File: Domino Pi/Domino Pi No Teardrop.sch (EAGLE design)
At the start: 63 parts, among them J1 MH28-1, J2 MH28-1, M1 DOMINO, SW1 IT-1100, U1 MP2162GQH, U2 CP2104-F03-GM, U3 74LVC1G125DCK

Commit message: Changed copyright
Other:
- note added: "The Domino Team may make changes to specifications and product"
- note added: "© 2014, The Domino Team All rights reserved."
- note removed: "Michel Stempin may make changes to specifications and product"
- note removed: "© 2014, Michel Stempin All rights reserved."
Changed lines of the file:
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@@
 <layer number="102" name="CC-BY-SA_Letters" color="0" fill="4" visible="yes" active="yes"/>
 <layer number="103" name="CC-BY-SA_Filling" color="15" fill="1" visible="yes" active="yes"/>
+<layer number="107" name="legend" color="7" fill="1" visible="yes" active="yes"/>
+<layer number="108" name="Module_Measures" color="7" fill="1" visible="yes" active="yes"/>
 <layer number="119" name="mUnrouted" color="7" fill="1" visible="no" active="no"/>
 <layer number="126" name="mbNames" color="7" fill="1" visible="no" active="no"/>
@@
 <text x="302.26" y="12.7" size="0.8128" layer="94">Reference designs are provided "AS IS" and "WITH ALL FAULTS".</text>
 <text x="302.26" y="10.16" size="0.8128" layer="94">regarding this product, including but not limited to, any implied warranties of</text>
-<text x="302.26" y="6.35" size="0.8128" layer="94">Michel Stempin may make changes to specifications and product </text>
+<text x="302.26" y="6.35" size="0.8128" layer="94">The Domino Team may make changes to specifications and product </text>
 <text x="302.26" y="11.43" size="0.8128" layer="94">Global Marine Networks disclaims all other warranties express or implied, </text>
 <text x="302.26" y="8.89" size="0.8128" layer="94">merchantibility or fitness for any particular application.</text>
 <text x="302.26" y="5.08" size="0.8128" layer="94">descriptions at any time, without notice.</text>
-<text x="345.44" y="20.32" size="1.27" layer="94">© 2014, Michel Stempin
+<text x="345.44" y="20.32" size="1.27" layer="94">© 2014, The Domino Team
 All rights reserved.</text>
 <text x="379.222" y="5.334" size="1.778" layer="94">&gt;REV</text>

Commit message: Domino Pi rev. C: removed Schottky diode on +VUSB, it causes too much voltage drop, optimized power wiring, changed Logos
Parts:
- removed D4: BLUE, Domino:LED_0603
- added U$7: DOMINO_PI_LOGO, Domino:DOMINO_PI_LOGO
- A1: value ACA-5036-A2-CC-S -> RF_ANT1; device Domino:ACA-5036-A2-CC-S -> Domino:RF_ANT1; BOM (none) -> EXCLUDE; PARTNO (none) -> WIFI_ANT-2.4GHz
- D1: value MBRM130LT1G -> PRTR5V0U2X; device Domino:MBRM130LT1G -> Domino:PRTR5V0U2X; PARTNO MBRM130LT1G -> PRTR5V0U2X; RATE 1A -> 300W; VOLT 30V -> 5V
- D2: value PRTR5V0U2X -> RED; device Domino:PRTR5V0U2X -> Domino:LED_0402; PARTNO PRTR5V0U2X -> LED0402-RED; RATE 300W -> (none); VOLT 5V -> (none)
- D3: value RED -> BLUE; device Domino:LED_0603 -> Domino:LED_0402; PARTNO LED0603-RED -> LED0402-BLUE
- R13: value 1k -> 10k; PARTNO R0402_1k_5%_62.5mW -> R0402_10k_5%_62.5mW
- R14: value 10k -> 1k; PARTNO R0402_10k_5%_62.5mW -> R0402_1k_5%_62.5mW
- S1: value USB_MR5-003A -> USB_MR5-001; device Domino:USB_MR5-003A -> Domino:USB_MR5-001; PARTNO USB MR5-003A -> USB MR5-001
- SW1: value IT-1100 -> IT-1210; device Domino:IT-1100 -> Domino:IT-1210; PARTNO IT-1100 -> IT-1210
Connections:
- removed net +VUSB: D1.A, L1.1
- net +2V5: now also R14.2; no longer R13.2
- net +5V: now also L1.1; no longer D1.C
- net ANT0_50R: now also A1.FEED; no longer A1.A
- net BLUE_LED: now also D3.A; no longer D4.A
- net D+: now also D1.P$2; no longer D2.P$3
- net D-: now also D1.P$3; no longer D2.P$2
- net GND: now also A1.GND, D1.P$1, D2.C, R13.1; no longer A1.GND@1, A1.GND@2, D2.P$1, D4.C, R14.1
- net JUMPSTART: now also R14.1, SW1.1; no longer R13.1, SW1.2
- net N$1: now also D2.A; no longer D3.A
- net PE: now also S1.M3
- net UART_RTS: now also R13.2, SW1.2; no longer R14.2, SW1.1
- net VBUS: now also D1.P$4; no longer D2.P$4
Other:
- note removed: "Domino Core"
- note removed: "Domino Pi"
- note removed: "Domino Qi"
- moved on the sheet: C19, C20, C21, D3, R11, R12, R13, R14

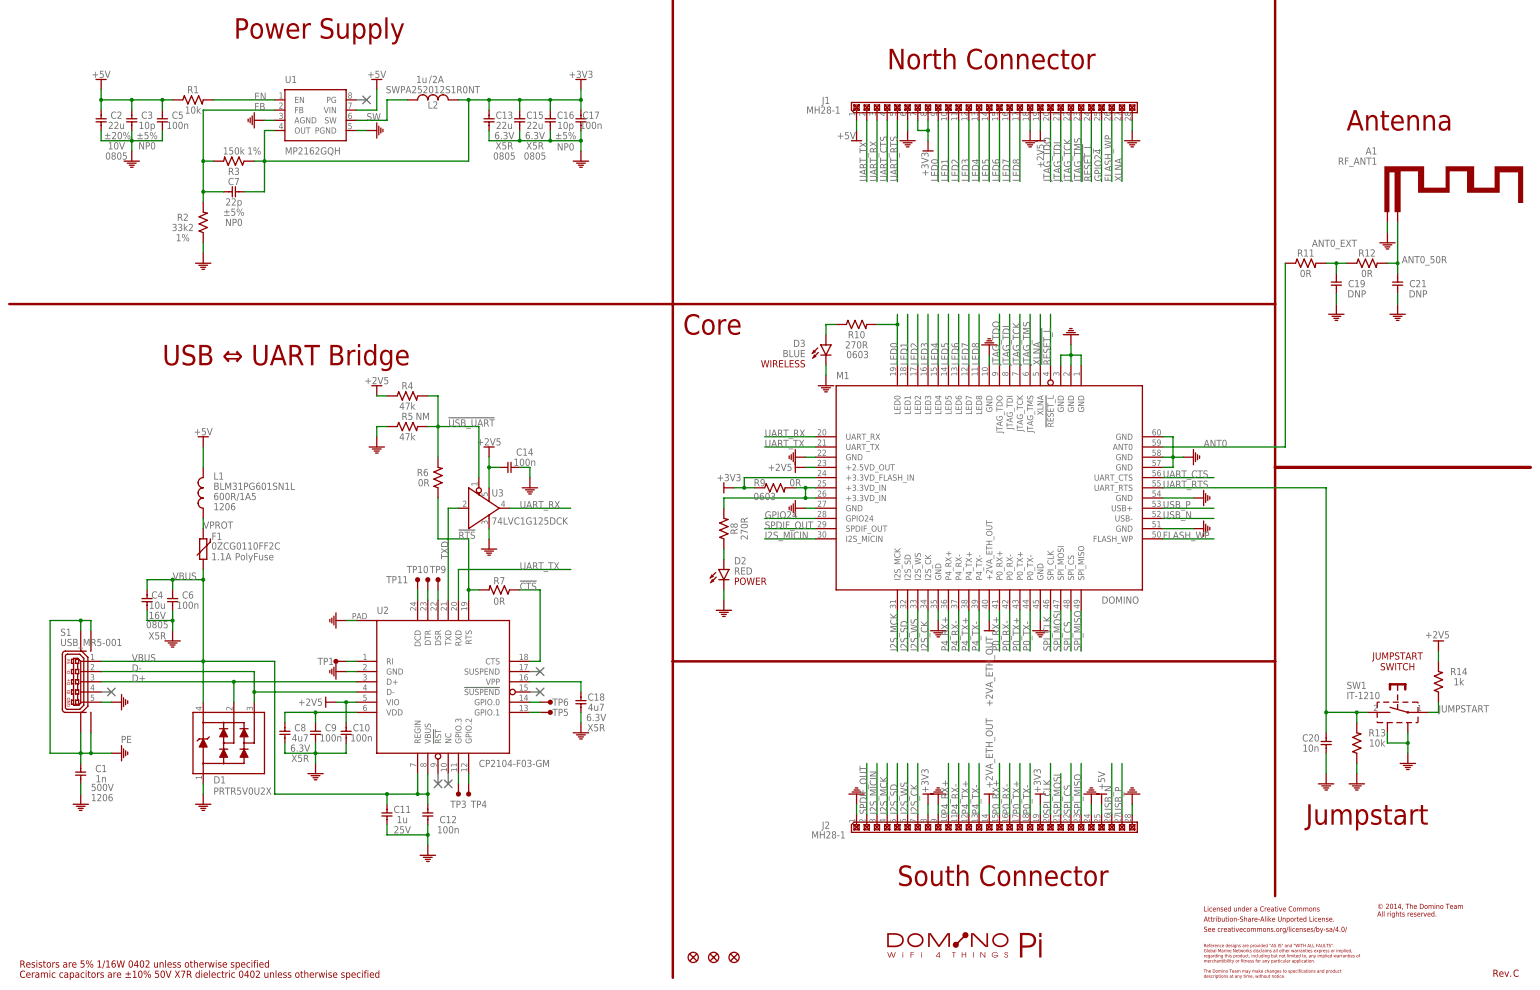
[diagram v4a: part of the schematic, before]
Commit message: Domino Pi Rev. D: replaced resetable fuse by power swich, mino changes DC/DC layout and added more stitching vias
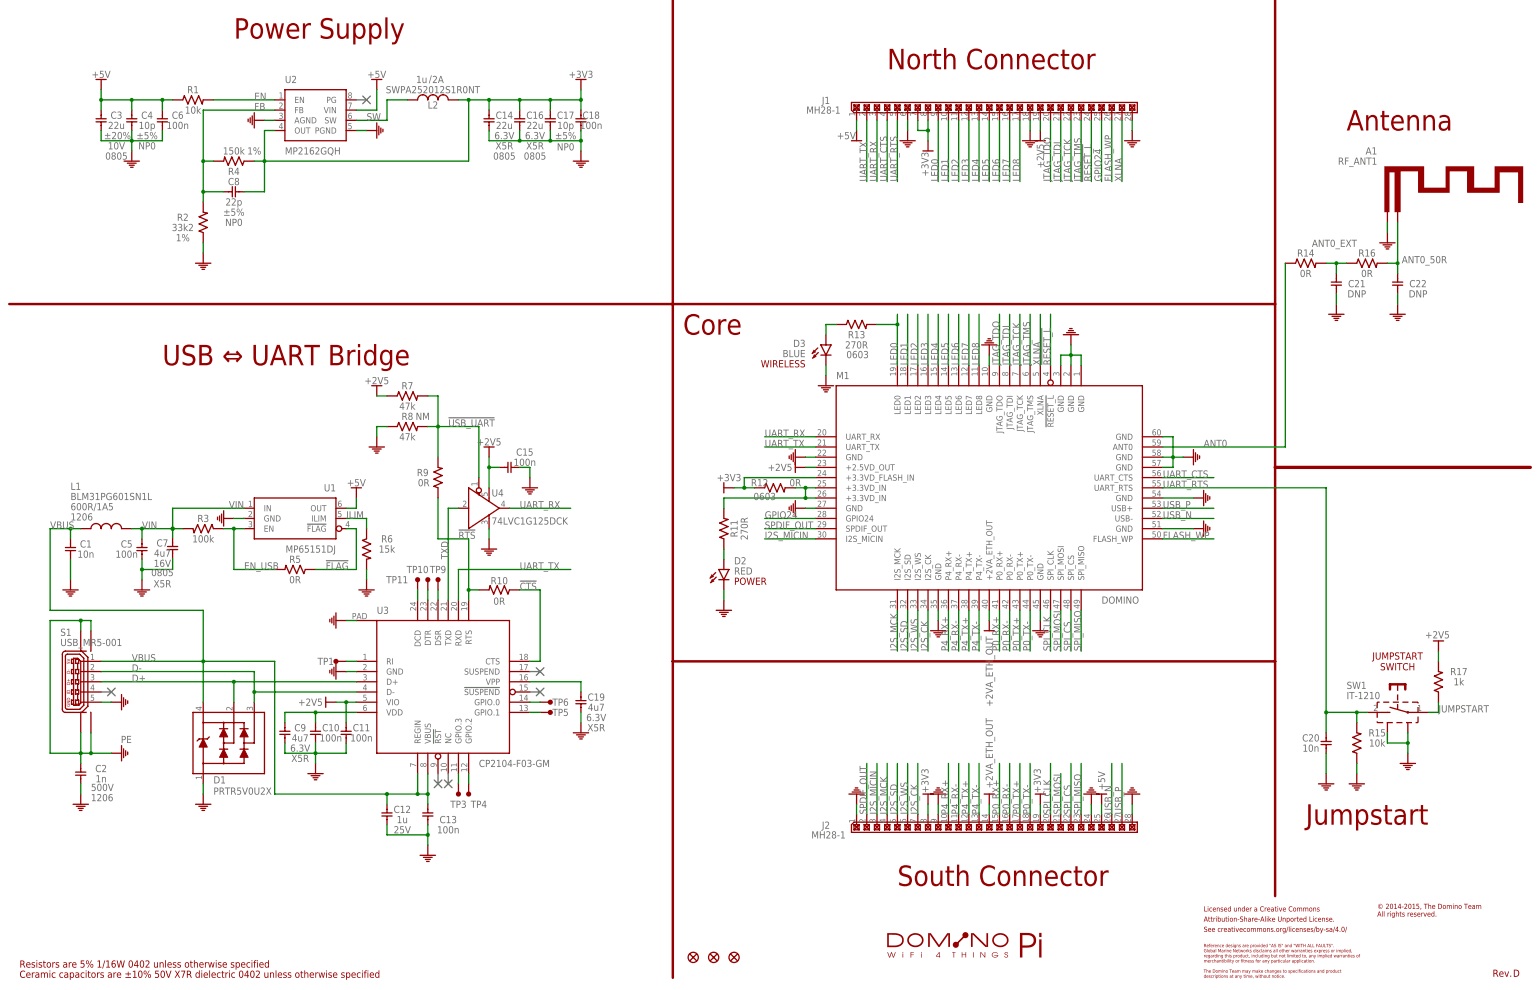
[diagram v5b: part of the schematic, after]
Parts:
- removed F4: FIDUCIAL, Domino:FIDUCIAL
- added C22: DNP, Domino:CAP_0402
- added R15: 10k, Domino:RES_0402
- added R16: 0R, Domino:RES_0402
- added R17: 1k, Domino:RES_0402
- added U4: 74LVC1G125DCK, Domino:74LVC1G125DCK
- C1: value 1n -> 10n; device Domino:CAP_1206 -> Domino:CAP_0402; PARTNO C1206_1n_X7R_10%_CER_500V -> C0402_10n_X7R_10%_CER_50V; VOLT 500V -> 50V
- C11: value 1u -> 100n; PARTNO C0402_1u_X7R_10%_CER_25V -> C0402_100n_X7R_10%_CER_50V; VOLT 25V -> 50V
- C12: value 100n -> 1u; PARTNO C0402_100n_X7R_10%_CER_50V -> C0402_1u_X7R_10%_CER_25V; VOLT 50V -> 25V
- C13, C15: value 22u -> 100n; device Domino:CAP_0805 -> Domino:CAP_0402; PARTNO C0805_22u_X5R_20%_CER_6V3 -> C0402_100n_X7R_10%_CER_50V; TC X5R -> X7R; TOL ±20% -> ±10%; VOLT 6.3V -> 50V
- C14: value 100n -> 22u; device Domino:CAP_0402 -> Domino:CAP_0805; PARTNO C0402_100n_X7R_10%_CER_50V -> C0805_22u_X5R_20%_CER_6V3; TC X7R -> X5R; TOL ±10% -> ±20%; VOLT 50V -> 6.3V
- C16: value 10p -> 22u; device Domino:CAP_0402 -> Domino:CAP_0805; PARTNO C0402_10p_NP0_5%_CER_50V -> C0805_22u_X5R_20%_CER_6V3; TC NP0 -> X5R; TOL ±5% -> ±20%; VOLT 50V -> 6.3V
- C17: value 100n -> 10p; PARTNO C0402_100n_X7R_10%_CER_50V -> C0402_10p_NP0_5%_CER_50V; TC X7R -> NP0; TOL ±10% -> ±5%
- C18: value 4u7 -> 100n; PARTNO C0402_4u7_X5R_10%_CER_6V3 -> C0402_100n_X7R_10%_CER_50V; TC X5R -> X7R; VOLT 6.3V -> 50V
- C19: value DNP -> 4u7; DNP T -> (none); PARTNO C0402_DNP -> C0402_4u7_X5R_10%_CER_6V3; TC (none) -> X5R; TOL (none) -> ±10%; TYPE (none) -> CER; VOLT (none) -> 6.3V
- C2: value 22u -> 1n; device Domino:CAP_0805 -> Domino:CAP_1206; PARTNO C1206_22u_X7R_20%_CER_10V -> C1206_1n_X7R_10%_CER_500V; TOL ±20% -> ±10%; VOLT 10V -> 500V
- C3: value 10p -> 22u; device Domino:CAP_0402 -> Domino:CAP_0805; PARTNO C0402_10p_NP0_5%_CER_50V -> C1206_22u_X7R_20%_CER_10V; TC NP0 -> X7R; TOL ±5% -> ±20%; VOLT 50V -> 10V
- C4: value 10u -> 10p; device Domino:CAP_0805 -> Domino:CAP_0402; PARTNO C0805_10u_X5R_10%_CER_16V -> C0402_10p_NP0_5%_CER_50V; TC X5R -> NP0; TOL ±10% -> ±5%; VOLT 16V -> 50V
- C7: value 22p -> 4u7; device Domino:CAP_0402 -> Domino:CAP_0805; PARTNO C0402_22p_NP0_5%_CER_50V -> C0805_4u7_X5R_10%_CER_16V; TC NP0 -> X5R; TOL ±5% -> ±10%; VOLT 50V -> 16V
- C8: value 4u7 -> 22p; PARTNO C0402_4u7_X5R_10%_CER_6V3 -> C0402_22p_NP0_5%_CER_50V; TC X5R -> NP0; TOL ±10% -> ±5%; VOLT 6.3V -> 50V
- C9: value 100n -> 4u7; PARTNO C0402_100n_X7R_10%_CER_50V -> C0402_4u7_X5R_10%_CER_6V3; TC X7R -> X5R; VOLT 50V -> 6.3V
- F1: value 0ZCG0110FF2C -> FIDUCIAL; device Domino:0ZCG0110FF2C -> Domino:FIDUCIAL; PARTNO 0ZCG0110FF2C -> (none)
- R10: value 270R -> 0R; device Domino:RES_0603 -> Domino:RES_0402; PARTNO R0603_270R_5%_125mW -> R0402_0R_5%_62.5mW
- R11: value 0R -> 270R; PARTNO R0402_0R_5%_62.5mW -> R0402_270R_5%_62.5mW
- R12: device Domino:RES_0402 -> Domino:RES_0603; PARTNO R0402_0R_5%_62.5mW -> R0603_0R_5%_125mW; RATE 62.5mW -> 125mW
- R13: value 10k -> 270R; device Domino:RES_0402 -> Domino:RES_0603; PARTNO R0402_10k_5%_62.5mW -> R0603_270R_5%_125mW; RATE 62.5mW -> 125mW
- R14: value 1k -> 0R; PARTNO R0402_1k_5%_62.5mW -> R0402_0R_5%_62.5mW
- R3: value 150k -> 100k; PARTNO R0402_150k_1%_62.5mW -> R0402_100k_5%_62.5mW; TOL 1% -> 5%
- R4: value 47k -> 150k; PARTNO R0402_47k_5%_62.5mW -> R0402_150k_1%_62.5mW; TOL 5% -> 1%
- R5: value 47k -> 0R; DNP T -> (none); PARTNO R0402_47k_5%_62.5mW -> R0402_0R_5%_62.5mW
- R6: value 0R -> 15k; PARTNO R0402_0R_5%_62.5mW -> R0402_15k_5%_62.5mW; RATE 125mW -> 62.5mW
- R7: value 0R -> 47k; PARTNO R0402_0R_5%_62.5mW -> R0402_47k_5%_62.5mW; RATE 125mW -> 62.5mW
- R8: value 270R -> 47k; DNP (none) -> T; PARTNO R0402_270R_5%_62.5mW -> R0402_47k_5%_62.5mW
- R9: device Domino:RES_0603 -> Domino:RES_0402; PARTNO R0603_0R_5%_125mW -> R0402_0R_5%_62.5mW
- U1: value MP2162GQH -> MP65151DJ; device Domino:MP2162GQH -> Domino:MP65151DJ; PARTNO MP2162GQH -> MP65151DJ
- U2: value CP2104-F03-GM -> MP2162GQH; device Domino:CP2104-F03-GM -> Domino:MP2162GQH; PARTNO CP2104-F03-GM -> MP2162GQH
- U3: value 74LVC1G125DCK -> CP2104-F03-GM; device Domino:74LVC1G125DCK -> Domino:CP2104-F03-GM; PARTNO 74LVC1G125DCK -> CP2104-F03-GM
- renumbered U$7 to W1
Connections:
- removed net VPROT: F1.1, L1.2
- new net !FLAG: R5.1, U1.!FLAG
- new net EN_USB: R3.1, R5.2, U1.EN
- new net ILIM: R6.1, U1.ILIM
- new net VIN: C5.1, C7.1, L1.1, R3.2, U1.IN
- net !CTS: now also R10.1, U3.CTS; no longer R7.1, U2.CTS
- net !RTS: now also R10.2, R9.1, U3.RTS; no longer R6.1, R7.2, U2.RTS
- net !USB_UART: now also R7.2, R8.2, R9.2, U4.!OE; no longer R4.2, R5.2, R6.2, U3.!OE
- net +2V5: now also C11.1, C15.2, R17.2, R7.1, U3.VIO, U4.VCC; no longer C10.1, C14.2, R14.2, R4.1, U2.VIO, U3.VCC
- net +3.3VD_IN: now also R11.2, R12.2; no longer R8.2, R9.2
- net +3V3: now also C14.1, C18.1, C8.2, R12.1, R4.1, U2.OUT; no longer C13.1, C15.1, C7.2, R3.1, R9.1, U1.OUT
- net +5V: now also C4.1, C6.1, U1.OUT, U2.VIN; no longer C2.1, C5.1, L1.1, U1.VIN
- net ANT0: now also R14.1; no longer R11.1
- net ANT0_50R: now also C22.1, R16.2; no longer C21.1, R12.2
- net ANT0_EXT: now also C21.1, R14.2, R16.1; no longer C19.1, R11.2, R12.1
- net BLUE_LED: now also R13.1; no longer R10.1
- net D+: now also U3.D+; no longer U2.D+
- net D-: now also U3.D-; no longer U2.D-
- net EN: now also U2.EN; no longer U1.EN
- net FB: now also C8.1, R4.2, U2.FB; no longer C7.1, R3.2, U1.FB
- net GND: now also C14.2, C15.1, C22.2, C7.2, R15.1, R6.2, R8.1, U1.GND, U2.AGND, U2.PGND, U3.PAD, U4.GND; no longer C14.1, C15.2, C8.2, R13.1, R5.1, U1.AGND, U1.PGND, U2.GND, U2.PAD
- net JUMPSTART: now also R17.1; no longer R14.1
- net LED0: now also R13.2; no longer R10.2
- net N$1: now also R11.1; no longer R8.1
- net N$12: now also U3.DTR; no longer U2.DTR
- net N$13: now also U3.DCD; no longer U2.DCD
- net N$15: now also U3.GPIO.0; no longer U2.GPIO.0
- net N$16: now also U3.GPIO.1; no longer U2.GPIO.1
- net N$2: now also U3.DSR; no longer U2.DSR
- net N$31: now also C19.1, U3.VPP; no longer C18.1, U2.VPP
- net N$6: now also U3.RI; no longer U2.RI
- net N$8: now also U3.GPIO.3; no longer U2.GPIO.3
- net N$9: now also U3.GPIO.2; no longer U2.GPIO.2
- net PE: now also C2.1; no longer C1.1
- net SW: now also U2.SW; no longer U1.SW
- net TXD: now also U3.TXD, U4.A; no longer U2.TXD, U3.A
- net UART_RTS: now also R15.2; no longer R13.2
- net UART_RX: now also U4.Y; no longer U3.Y
- net UART_TX: now also U3.RXD; no longer U2.RXD
- net VBUS: now also C1.1, C13.1, L1.2, U3.REGIN, U3.VBUS; no longer C11.1, C4.1, C6.1, F1.2, U2.REGIN, U2.VBUS
- net VDD: now also C10.1, U3.VDD; no longer C8.1, U2.VDD
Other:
- note added: "© 2014-2015, The Domino Team All rights reserved."
- note removed: "PolyFuse"
- note removed: "© 2014, The Domino Team All rights reserved."
- moved on the sheet: C1, C10, C11, C12, C13, C14, C15, C16, C17, C18, C19, C2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

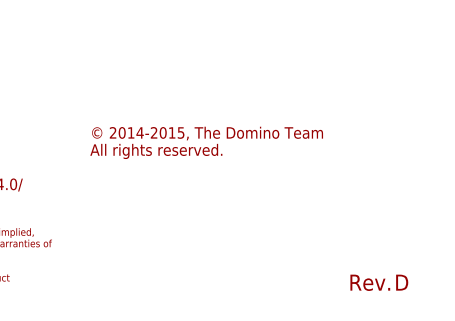
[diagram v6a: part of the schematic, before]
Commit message: Domnio Pi Rev. E: changed silkscreen font ratio to 20%
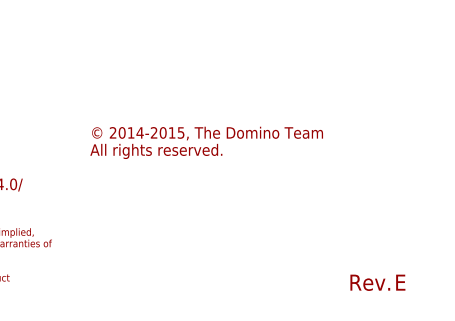
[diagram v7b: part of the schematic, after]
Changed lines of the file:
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@@
 <attribute name="DATABASE" value="./../Common/BOM/Domino_DB.txt"/>
 <attribute name="DRAWN" value="M.STEMPIN"/>
-<attribute name="REV" value="D"/>
+<attribute name="REV" value="E"/>
 </attributes>
 <variantdefs>
